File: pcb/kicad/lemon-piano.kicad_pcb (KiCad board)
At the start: 2 copper layers, 120 x 40 mm, 48 parts, among them J1 5V_IN, J2 LEMON_KEYS, J3 SENS+_EXT, J4 SENS-_EXT, SW1 SENS+, SW2 SENS-, U1 Nano_socket_A, U2 Nano_socket_B

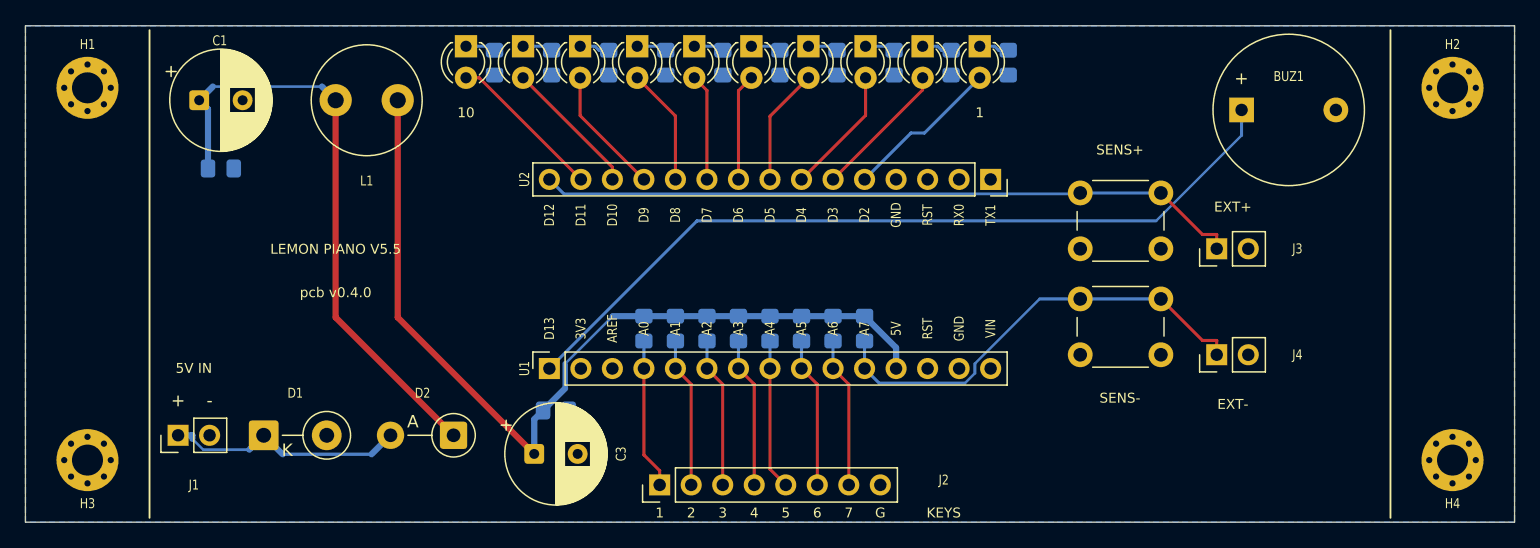
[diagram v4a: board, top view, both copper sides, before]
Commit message: feat(pcb): v0.5.0 — flip the Nano (USB east), keys north, LEDs south, filter refactored
Second pass on the 120x40 board, to the user's follow-up spec. The V5.5
circuit is unchanged; this is all orientation and placement.

- The Nano is FLIPPED 180 deg: mini-USB now faces EAST (ADR-029). This is
  the load-bearing change and it is what "keys up, LEDs down" REQUIRES: the
  module's analog and digital columns sit on opposite long edges, so the
  only way to change which board edge they face is to rotate the module.
  U1 (analog) becomes the NORTH row with pin 1 (D13) east; U2 (digital)
  becomes the SOUTH row with pin 1 (TX1) west.
- Keys header on the NORTH edge, still centred (pin centre exactly x=150),
  pin 1 = KEY1 at the EAST because A0..A6 now descend west->east. Silk
  reads KEYS G 7 6 5 4 3 2 1; the GND clip moved to the header's west end.
- LED bar on the SOUTH edge, centred on x=150, ascending west->east (LED1
  west under D2, LED10 east under D11) - the mirror of the old order.
- Both 0805 resistor groups INVERTED their pad numbers. The builder nets
  them geometrically, so the pull-ups (now south of a north analog row) and
  the LED resistors (now north of a south bar) both swapped which pad
  carries which net. ground-truth/components.yaml was re-derived from the
  built board; two new assertions pin the KEY pad at y=114.6 and the LED
  cathode pad at y=138.03 so this cannot drift silently.
- USB-cable keepout dropped (ADR-030) at the user's explicit request.
  Stated plainly: the USB shell now reaches x~173.3 with SW1's courtyard at
  173.48, so FLASHING MEANS LIFTING THE NANO OUT OF ITS SOCKET. That is the
  direct cost of keys-north + LEDs-south, not an oversight.
- Filter section refactored into a compact 3-row west block (ADR-031) now
  that the corridor no longer punches a hole through it: C1 || C3 ADJACENT
  on the north row as asked, D2 -> L1 on the middle row with their pads
  5.5 mm apart, J1 -> D1 on the south row. Both bulk caps are now ~13 mm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
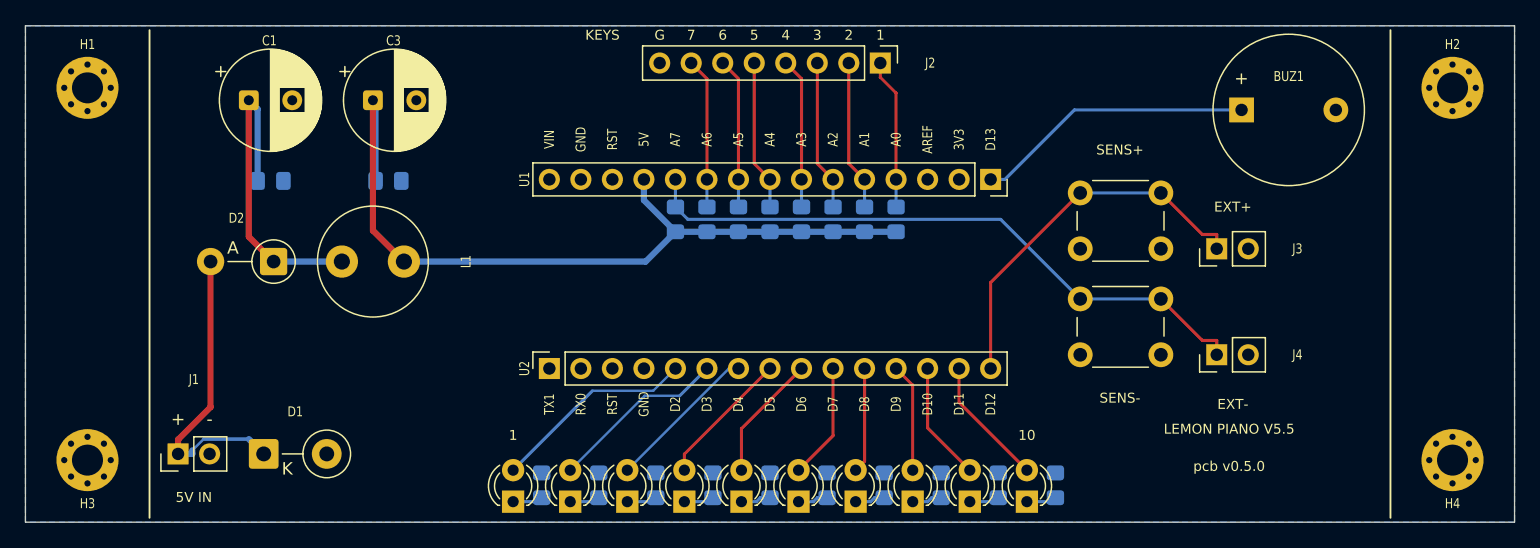
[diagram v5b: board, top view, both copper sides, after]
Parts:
- moved D12 58.2 mm to (170.7, 138.3), turned to 90 degrees
- moved R17 56.6 mm to (173.0, 137.0)
- moved D3 52.5 mm to (129.3, 138.3), turned to 90 degrees
- moved D11 51.4 mm to (166.1, 138.3), turned to 90 degrees
- moved R8 50.7 mm to (131.6, 137.0)
- moved R16 49.6 mm to (168.4, 137.0)
- moved D4 46.4 mm to (133.9, 138.3), turned to 90 degrees
- moved D10 45.4 mm to (161.5, 138.3), turned to 90 degrees
- moved R9 44.3 mm to (136.2, 137.0)
- moved R15 43.3 mm to (163.8, 137.0)
- moved D5 41.4 mm to (138.5, 138.3), turned to 90 degrees
- moved D9 40.7 mm to (156.9, 138.3), turned to 90 degrees
- moved R10 39.1 mm to (140.8, 137.0)
- moved U1 38.7 mm to (167.8, 112.4), turned to -90 degrees
- moved U2 38.7 mm to (132.2, 127.6), turned to 90 degrees
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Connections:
- R1 pad 1: /KEY1 -> /+5V
- R1 pad 2: /+5V -> /KEY1
- R10 pad 1: /GND -> /LED3_K
- R10 pad 2: /LED3_K -> /GND
- R11 pad 1: /GND -> /LED4_K
- R11 pad 2: /LED4_K -> /GND
- R12 pad 1: /GND -> /LED5_K
- R12 pad 2: /LED5_K -> /GND
- R13 pad 1: /GND -> /LED6_K
- R13 pad 2: /LED6_K -> /GND
- R14 pad 1: /GND -> /LED7_K
- R14 pad 2: /LED7_K -> /GND
- R15 pad 1: /GND -> /LED8_K
- R15 pad 2: /LED8_K -> /GND
- R16 pad 1: /GND -> /LED9_K
- R16 pad 2: /LED9_K -> /GND
- R17 pad 1: /GND -> /LED10_K
- R17 pad 2: /LED10_K -> /GND
- R18 pad 1: /SENS_MINUS -> /+5V
- R18 pad 2: /+5V -> /SENS_MINUS
- R2 pad 1: /KEY2 -> /+5V
- R2 pad 2: /+5V -> /KEY2
- R3 pad 1: /KEY3 -> /+5V
- R3 pad 2: /+5V -> /KEY3
- R4 pad 1: /KEY4 -> /+5V
- R4 pad 2: /+5V -> /KEY4
- R5 pad 1: /KEY5 -> /+5V
- R5 pad 2: /+5V -> /KEY5
- R6 pad 1: /KEY6 -> /+5V
- R6 pad 2: /+5V -> /KEY6
- R7 pad 1: /KEY7 -> /+5V
- R7 pad 2: /+5V -> /KEY7
- R8 pad 1: /GND -> /LED1_K
- R8 pad 2: /LED1_K -> /GND
- R9 pad 1: /GND -> /LED2_K
- R9 pad 2: /LED2_K -> /GND
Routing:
- net /BUZZER: track 65.6 -> 22.5 mm
- net /SENS_PLUS: track 56.8 -> 30.7 mm
- net /VRAW: track 48.6 -> 26.1 mm
- net /SENS_MINUS: track 36.9 -> 51.4 mm
- net /+5V: track 72.3 -> 66.5 mm
- net /VIN: track 19.5 -> 24.6 mm
- net /LED1: track 12.7 -> 16.5 mm
- net /LED2: track 11.2 -> 14.4 mm
- net /LED10: track 12.7 -> 10.5 mm
- net /LED3: track 10.3 -> 12.4 mm
- net /LED5: track 8.62 -> 10.2 mm
- net /LED4: track 9.47 -> 11.0 mm
- net /LED9: track 11.2 -> 9.60 mm
- net /LED8: track 10.3 -> 8.75 mm
- net /LED7: track 9.47 -> 8.49 mm
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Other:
- board text added: "pcb v0.5.0"
- board text removed: "pcb v0.4.0"

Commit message: fix(pcb): v0.5.1 — restore D1's 3D body (Kathode/Cathode filename split)
User-reported: D1 had no body in any realistic render, just bare pads and
silk, while D2 right beside it rendered fine.

Cause: KiCad 9's Diode_THT:D_DO-15_P5.08mm_Vertical_KathodeUp footprint
references a STEP of the same name, but kicad-packages3D ships that body
spelled the English way, D_DO-15_P5.08mm_Vertical_CathodeUp.step. The
footprint kept the legacy German-ish "Kathode"; the 3D library moved to
"Cathode", so the path resolved to nothing. kicad-cli pcb render skips
models it cannot resolve SILENTLY - no warning, no DRC item, no build error
- which is why it survived unnoticed from v0.3.0 (first release with 3D
bodies) through v0.5.0. D2 was unaffected because its footprint and model
names agree (..._AnodeUp), no K/C discrepancy.

Fix: point D1 at the file that exists, reusing the per-footprint override
already there for the coloured LEDs. LED_MODELS is folded into a general
MODEL_OVERRIDES table, and the override loop now raises if a target
footprint has no (model ...) block to patch, so a future library change
fails loudly instead of silently reverting to no body. Verified in the
render: D1 shows the vertical DO-15 cylinder with its lead bent to the
square cathode pad, occluding its own pads exactly like D2 and L1.

Scope: COSMETIC ONLY. 3D models take no part in gerbers, drill files, BOM,
position files, the netlist or DRC, so v0.5.0's fabrication package was
never wrong - only its renders were incomplete. Hence a PATCH bump.

Audited all 44 model paths the board references against upstream
kicad-packages3D while in there. Three others are absent upstream but
resolve on the render host and render correctly, so no action needed: L1's
Fastron choke and the two LED_D3.0mm_Orange.step bodies (service-shipped
per ADR-021). D1 was the only broken reference.

AGENT_PROMPT gains the lesson: a missing 3D body is invisible to every
automated gate this project has, so the render-inspection step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
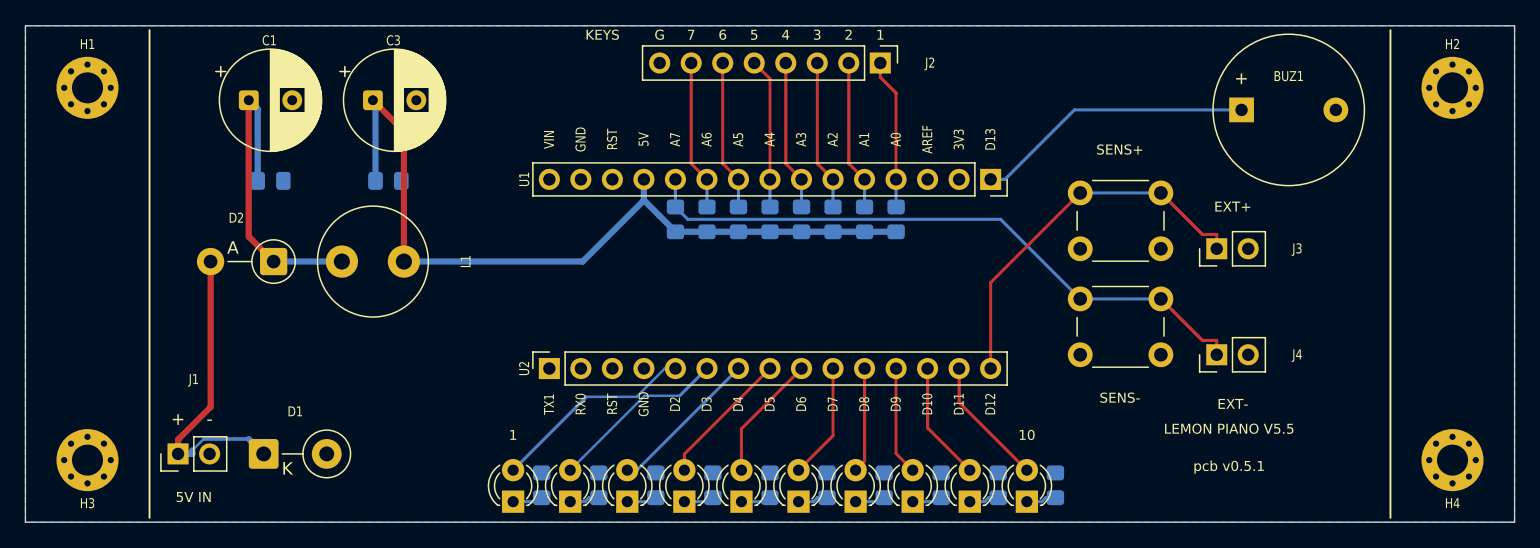
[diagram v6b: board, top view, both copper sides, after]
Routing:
- net /+5V: track 66.5 -> 65.1 mm
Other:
- board text added: "pcb v0.5.1"
- board text removed: "pcb v0.5.0"

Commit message: feat(pcb): v0.6.0 — J5, 2-pin aux speaker output in parallel with the buzzer
User request: two pins for an external speaker.

- New 2-pin header J5 (silk "SPK") on the SAME two nodes as the buzzer:
  pad 1 on /BUZZER (the D13 drive line), pad 2 on /GND. Placed immediately
  west of BUZ1 with a 5.18 mm courtyard gap, same pattern as the SENS
  external-button headers (ADR-026). Nothing is switched or cut - the
  on-board buzzer keeps sounding and whatever is plugged into J5 sees
  exactly the same signal.

- LOAD LIMIT, documented in ADR-034 and the README assembly notes. The
  buzzer is a PASSIVE piezo driven straight off the pin ("no series
  resistor needed", versions/v0-buzzer/HARDWARE.md), i.e. a high-impedance
  load of a few mA. A bare 4-8 ohm dynamic voice coil is not: at 5 V it
  would ask for roughly 600 mA against the ATmega328P's 40 mA absolute
  maximum (20 mA recommended) per pin, and would damage D13. J5 is
  therefore rated for another piezo element or an AMPLIFIED speaker module
  (PAM8403 / LM386 / powered PC speakers - all high-impedance inputs); a
  raw speaker only through an amplifier.

  No series resistor or amplifier was added to the board: the sources
  define a directly-driven passive buzzer, and inventing parts or values no
  source specifies is against the project's rules. A driver stage is a
  versions/ circuit change first, not a PCB-layer improvisation.

- geometry_gate gains a check that J5 stays adjacent to the buzzer it
  parallels (28 checks now). verify_placement covers 74 pad-net-function
  pairs (was 73). Schematic is 48 symbols (was 47).

- Fixed a pre-existing documentation error found while editing NETLIST.md:
  the U1/U2 rows in the component table had their descriptions swapped. U1
  is the ANALOG column (D13,3V3,AREF,A0..A7,5V,RST,GND,VIN), U2 the DIGITAL
  one (TX1,RX0,RST,GND,D2..D12). The pad-net tables and the ground truth
  were always right; only that table's prose was wrong.

Verification on the committed board: DRC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
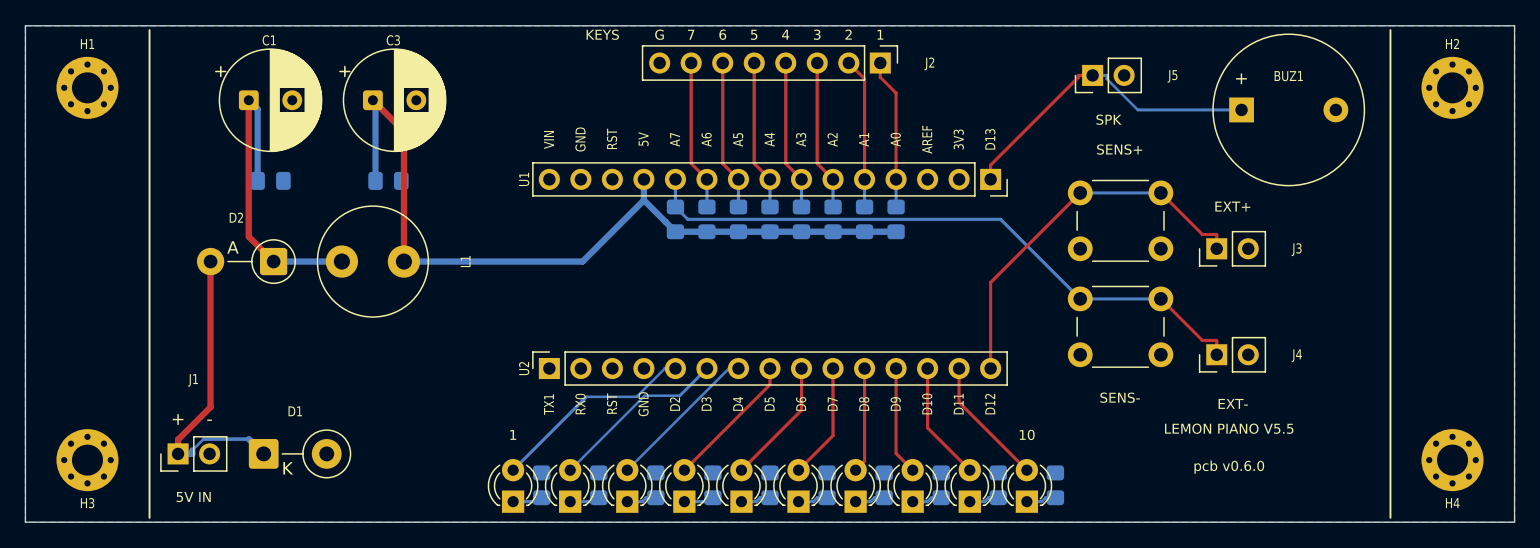
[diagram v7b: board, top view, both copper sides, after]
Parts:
- added L1: 100uH, L_Radial_D8.7mm_P5.00mm_Fastron_07HCP, F.Cu at (115.5, 119.0)
- J5: renamed from L1; value 100uH -> SPK_OUT; footprint L_Radial_D8.7mm_P5.00mm_Fastron_07HCP -> PinHeader_1x02_P2.54mm_Vertical
- moved J5 62.3 mm to (176.0, 104.0), turned to 90 degrees
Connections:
- J5 pad 1: /VRAW -> /BUZZER
- J5 pad 2: /+5V -> /GND
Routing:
- net /BUZZER: track 22.5 -> 25.8 mm
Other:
- board text added: "SPK"
- board text added: "pcb v0.6.0"
- board text removed: "pcb v0.5.1"

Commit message: feat(pcb): v0.7.0 — Nano turned back to USB-WEST for enclosure cable access
The user wants the mini-USB to leave the board on the left, away from the
SENS buttons, so the cable can be plugged in with the Nano seated once the
enclosure exists (annotated screenshot of the v0.6.0 render). Since the
Nano's pinout is fixed (ADR-015), USB-west means digital column north /
analog column south, so the LED bar moves to the north edge and the keys
header to the south edge in the same change.

Board (ADR-035/036/037):
- U1 analog = SOUTH row, pin 1 D13 west (rot 90); U2 digital = NORTH row,
  pin 1 TX1 east (rot 270). D12/D13 flank the USB at x=132.22.
- LED bar north, centred, LED1 at the EAST (follows D2..D11, which descend
  west->east -> non-crossing fan). Keys header south, centred, KEY1 at the
  WEST (follows A0..A6). Silk reads "KEYS 1 2 3 4 5 6 7 G".
- USB-cable corridor reinstated (x<130.4, y 113..127 part-free on F.Cu),
  supersedes ADR-030; geometry_gate enforces it against real courtyards.
- Filter folded around it: C1||C3 stay adjacent north; D2 -> (107.0,129.2),
  J1 -> D1 at y=136.0, L1 in its own column at (120.0,134.5).
- Both 0805 groups inverted pad numbers again; builder assertions moved
  (KEY pad y=125.4, cathode pad y=101.97), components.yaml re-derived from
  the built board.

Verification: /drc 0 errors / 0 warnings / 0 unconnected; ERC 0/0;
verify_placement 74 OK; verify_holes geometric + vision PASS (LOO 0.022 mm);
geometry_gate 30/30 incl. the corridor check; independent logical pass over
the routed board (pin->net map, monotonic fans, empty corridor, copper on
all nets, legend order); all 8 renders inspected (overlay USB-west, every
part has a 3D body); build_board byte-stable across two runs.

Release: pcb/releases/v0.7.0/lemon-piano-v0.7.0-fab.zip (14 files) from
/fab on the exact verified board. 3D models, renders, validation archived;
renders/INDEX.md regenerated. Docs: ADR-035..037, NETLIST, DESIGN_STATE,
pcb/README, AGENT_PROMPT, CHANGELOG.

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
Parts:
- moved D12 55.3 mm to (129.3, 101.7), turned to -90 degrees
- moved D3 55.3 mm to (170.7, 101.7), turned to -90 degrees
- moved R17 53.6 mm to (131.6, 103.0)
- moved R8 53.6 mm to (173.0, 103.0)
- moved D11 48.8 mm to (133.9, 101.7), turned to -90 degrees
- moved D4 48.8 mm to (166.1, 101.7), turned to -90 degrees
- moved R16 46.9 mm to (136.2, 103.0)
- moved R9 46.9 mm to (168.4, 103.0)
- moved D10 43.3 mm to (138.5, 101.7), turned to -90 degrees
- moved D5 43.3 mm to (161.5, 101.7), turned to -90 degrees
- moved R10 41.1 mm to (163.8, 103.0)
- moved R15 41.1 mm to (140.8, 103.0)
- moved D6 39.2 mm to (156.9, 101.7), turned to -90 degrees
- moved D9 39.2 mm to (143.1, 101.7), turned to -90 degrees
- moved U1 38.7 mm to (132.2, 127.6), turned to 90 degrees
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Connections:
- R1 pad 1: /+5V -> /KEY1
- R1 pad 2: /KEY1 -> /+5V
- R10 pad 1: /LED3_K -> /GND
- R10 pad 2: /GND -> /LED3_K
- R11 pad 1: /LED4_K -> /GND
- R11 pad 2: /GND -> /LED4_K
- R12 pad 1: /LED5_K -> /GND
- R12 pad 2: /GND -> /LED5_K
- R13 pad 1: /LED6_K -> /GND
- R13 pad 2: /GND -> /LED6_K
- R14 pad 1: /LED7_K -> /GND
- R14 pad 2: /GND -> /LED7_K
- R15 pad 1: /LED8_K -> /GND
- R15 pad 2: /GND -> /LED8_K
- R16 pad 1: /LED9_K -> /GND
- R16 pad 2: /GND -> /LED9_K
- R17 pad 1: /LED10_K -> /GND
- R17 pad 2: /GND -> /LED10_K
- R18 pad 1: /+5V -> /SENS_MINUS
- R18 pad 2: /SENS_MINUS -> /+5V
- R2 pad 1: /+5V -> /KEY2
- R2 pad 2: /KEY2 -> /+5V
- R3 pad 1: /+5V -> /KEY3
- R3 pad 2: /KEY3 -> /+5V
- R4 pad 1: /+5V -> /KEY4
- R4 pad 2: /KEY4 -> /+5V
- R5 pad 1: /+5V -> /KEY5
- R5 pad 2: /KEY5 -> /+5V
- R6 pad 1: /+5V -> /KEY6
- R6 pad 2: /KEY6 -> /+5V
- R7 pad 1: /+5V -> /KEY7
- R7 pad 2: /KEY7 -> /+5V
- R8 pad 1: /LED1_K -> /GND
- R8 pad 2: /GND -> /LED1_K
- R9 pad 1: /LED2_K -> /GND
- R9 pad 2: /GND -> /LED2_K
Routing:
- net /BUZZER: track 25.8 -> 79.4 mm, vias 0 -> 1
- net /SENS_PLUS: track 30.7 -> 56.8 mm
- net /VRAW: track 26.1 -> 45.6 mm
- net /+5V: track 65.1 -> 81.5 mm
- net /SENS_MINUS: track 51.4 -> 36.9 mm
- net /VIN: track 24.6 -> 15.0 mm
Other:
- board text added: "pcb v0.7.0"
- board text removed: "pcb v0.6.0"
